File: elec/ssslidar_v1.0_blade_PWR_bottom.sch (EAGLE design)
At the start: 25 parts, among them P10 PIN_SMD_1X1_RECT, P11 PIN_SMD_1X2, P12 PIN_SMD_1X1_RECT, P13 PIN_SMD_1X1_RECT, P15 PIN_SMD_0.8X1_RECT, P16 PIN_SMD_1X1_RECT, P17 PIN_SMD_1X2, P18 PIN_SMD_0.8X1_RECT, P19 PIN_SMD_0.8X1_RECT, P2 PIN_SMD_1X1_RECT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

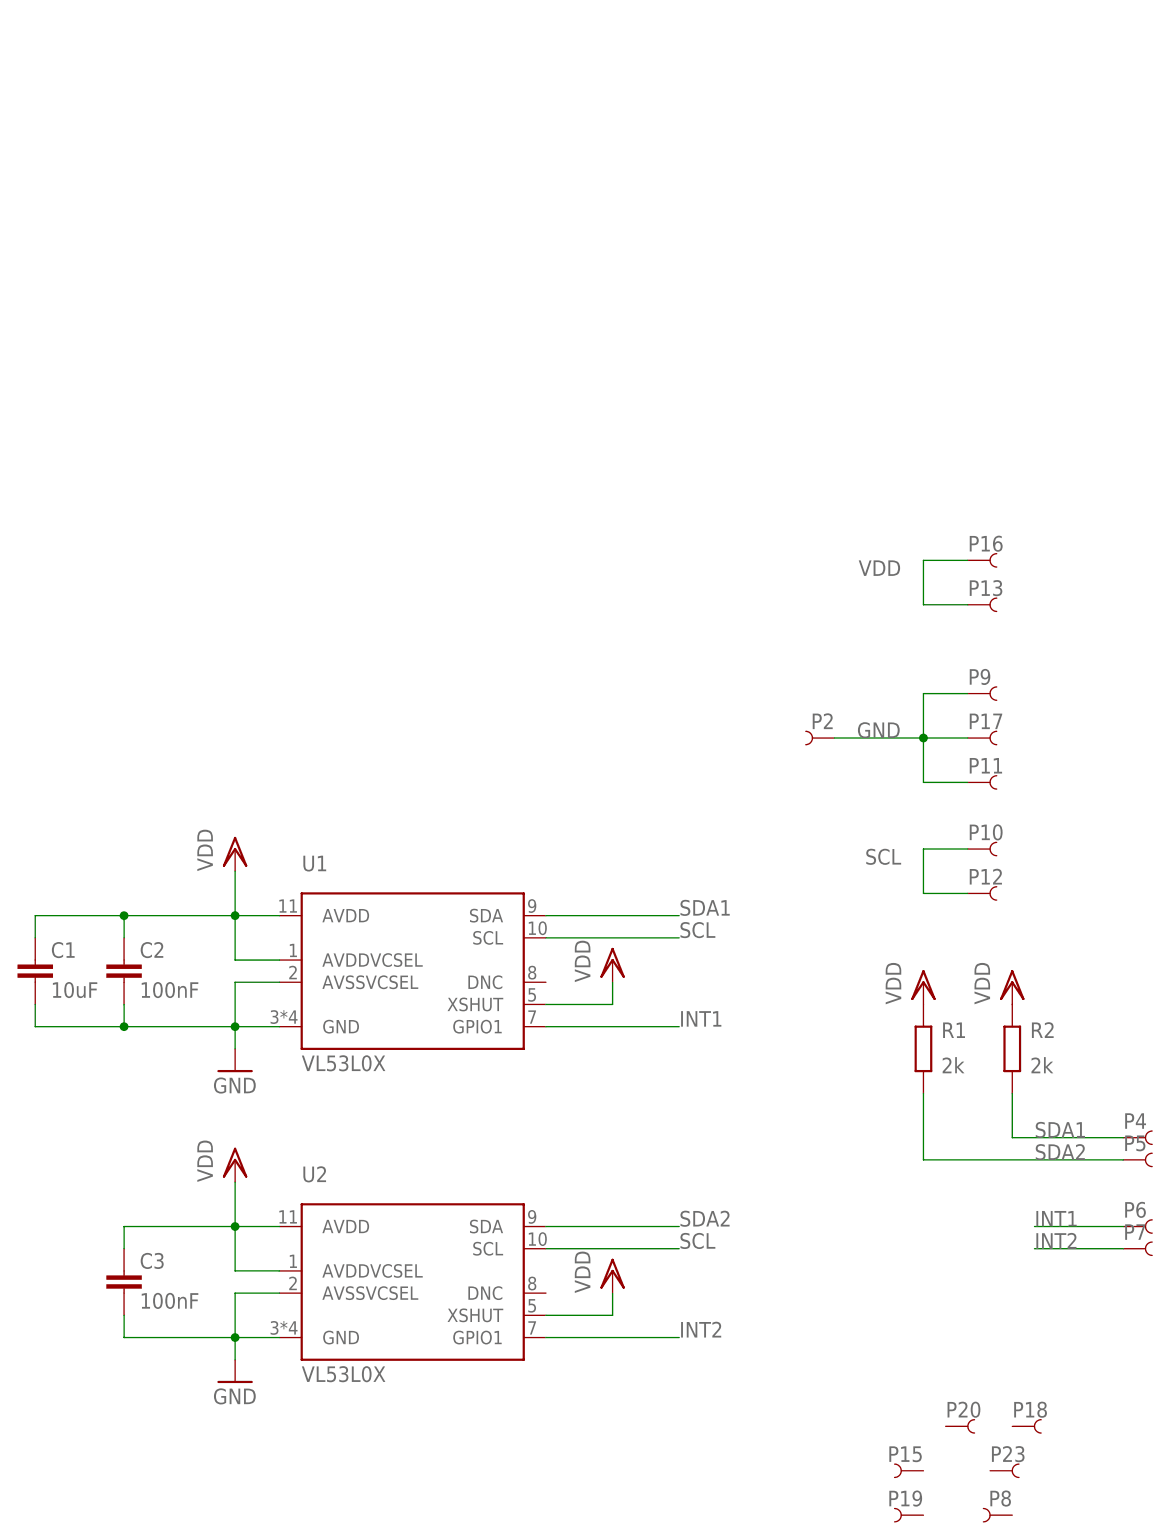
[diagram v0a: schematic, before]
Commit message: Separated blades into bottom and top, since the bottom ones need to be taller to avoid seeing the Main PCB, or the screws...
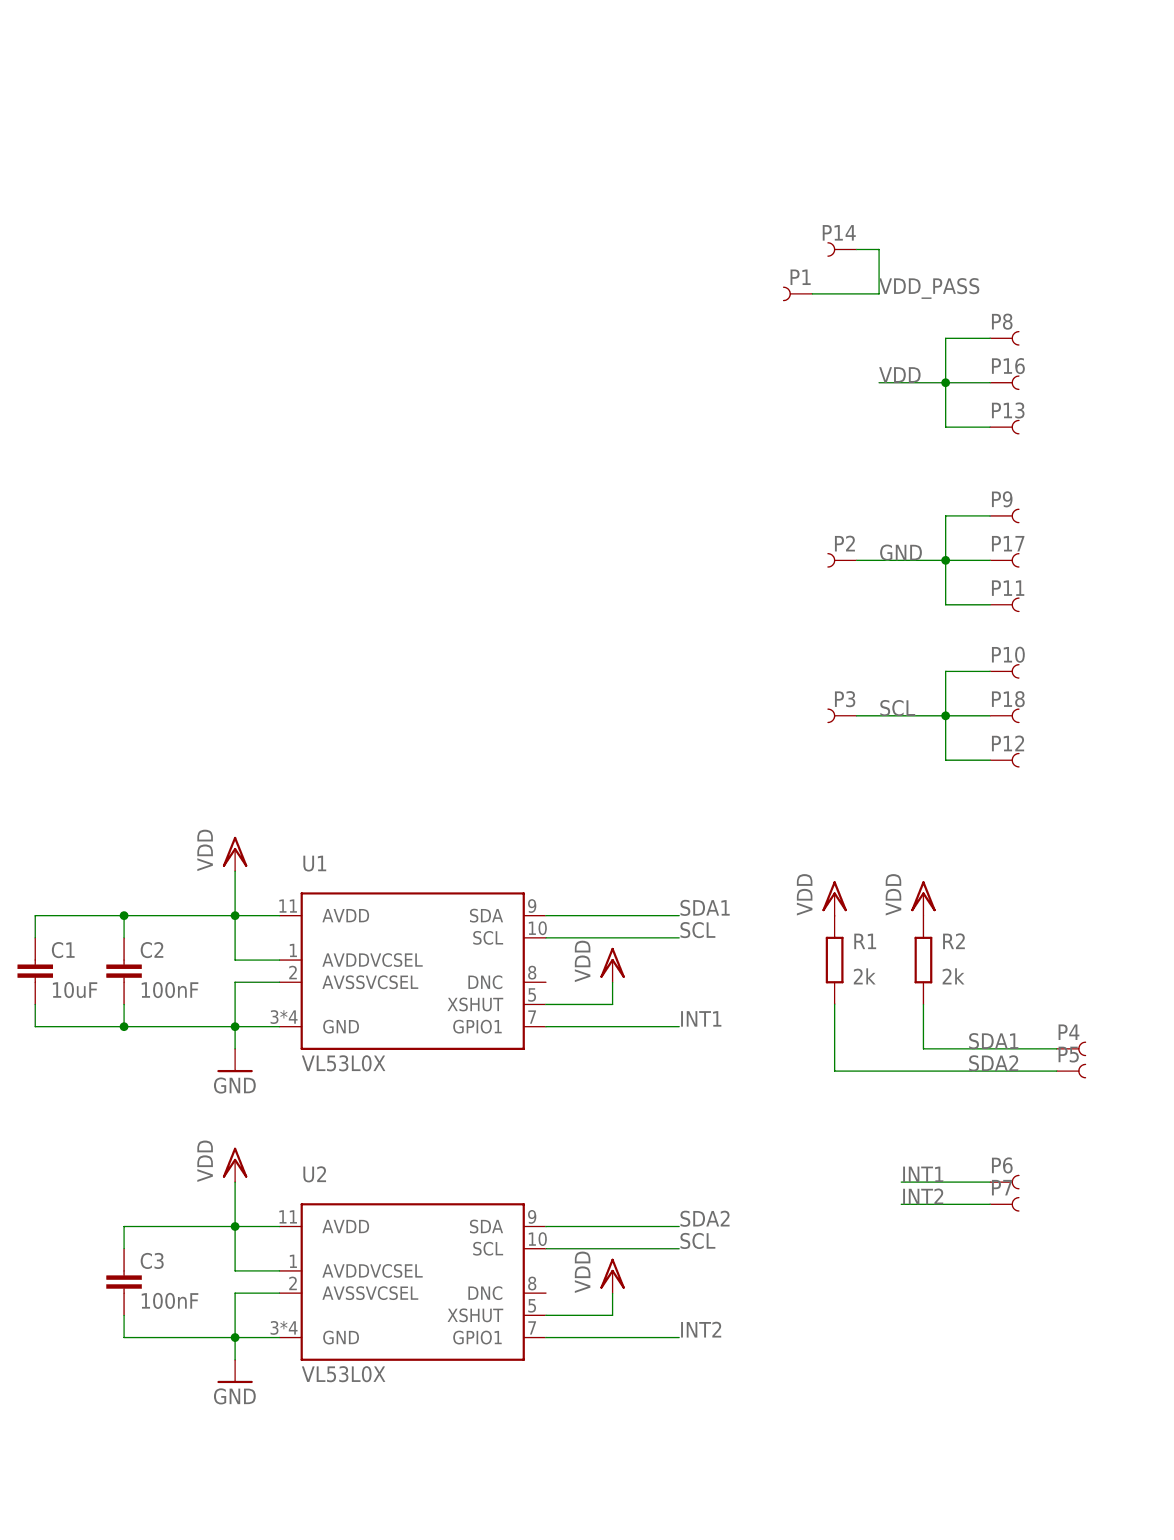
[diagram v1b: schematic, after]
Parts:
- removed P15, P19, P20, P23: PIN_SMD_0.8X1_RECT, Xevelabs:PIN_SMD_0.8X1_RECT
- added P1, P14, P3: PIN_SMD_0.8X1_RECT, Xevelabs:PIN_SMD_0.8X1_RECT
- P10, P12, P13, P16, P2, P9: value PIN_SMD_1X1_RECT -> PIN_SMD_1X2; device Xevelabs:PIN_SMD_1X1_RECT -> Xevelabs:PIN_SMD_1X2
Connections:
- new net VDD_PASS: P1.1, P14.1
- net SCL: now also P18.1, P3.1
- net VDD: now also P8.1
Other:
- moved on the sheet: P10, P11, P12, P13, P16, P17, P18, P2, P4, P5, P6, P7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

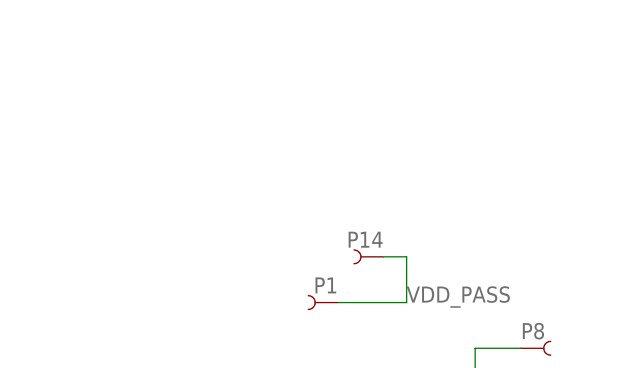
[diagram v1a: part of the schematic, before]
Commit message: Blades redesign done.
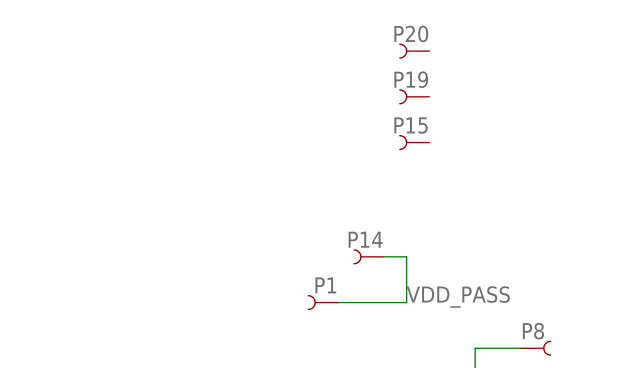
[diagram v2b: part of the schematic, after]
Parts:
- added P15, P19, P20: PIN_SMD_0.8X1_RECT, Xevelabs:PIN_SMD_0.8X1_RECT
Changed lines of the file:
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@@
 <part name="P14" library="Xevelabs" deviceset="PIN" device="_SMD_0.8X1_RECT" value="PIN_SMD_0.8X1_RECT"/>
 <part name="C3" library="Xevelabs" deviceset="C" device="0402" value="100nF"/>
+<part name="P15" library="Xevelabs" deviceset="PIN" device="_SMD_0.8X1_RECT" value="PIN_SMD_0.8X1_RECT"/>
+<part name="P19" library="Xevelabs" deviceset="PIN" device="_SMD_0.8X1_RECT" value="PIN_SMD_0.8X1_RECT"/>
+<part name="P20" library="Xevelabs" deviceset="PIN" device="_SMD_0.8X1_RECT" value="PIN_SMD_0.8X1_RECT"/>
 </parts>
 <sheets>
@@
 <instance part="P14" gate="G$1" x="99.06" y="134.62" rot="MR0"/>
 <instance part="C3" gate="G$1" x="15.24" y="15.24"/>
+<instance part="P15" gate="G$1" x="104.14" y="147.32" rot="MR0"/>
+<instance part="P19" gate="G$1" x="104.14" y="152.4" rot="MR0"/>
+<instance part="P20" gate="G$1" x="104.14" y="157.48" rot="MR0"/>
 </instances>
 <busses>
